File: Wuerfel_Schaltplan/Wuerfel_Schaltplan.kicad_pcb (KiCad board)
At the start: 2 copper layers, 21 parts, among them SW1 SW_Push, SW2 SW_Push

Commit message: Finish PCB design
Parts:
- moved D1 68.3 mm to (97.3, 101.5), turned to 0 degrees
- moved D2 61.5 mm to (104.3, 101.5), turned to 0 degrees
- moved R1 58.2 mm to (118.8, 114.0), turned to 0 degrees
- moved D3 57.7 mm to (111.3, 101.5), turned to 0 degrees
- moved R2 51.3 mm to (118.8, 108.0), turned to 0 degrees
- moved D4 48.2 mm to (104.3, 92.0), turned to 0 degrees
- moved R3 44.0 mm to (118.8, 101.5), turned to 0 degrees
- moved D5 38.6 mm to (111.3, 82.5), turned to 0 degrees
- moved D6 38.3 mm to (104.3, 82.5), turned to 0 degrees
- moved D7 38.0 mm to (97.3, 82.5), turned to 0 degrees
- moved R4 33.9 mm to (118.8, 92.0), turned to 0 degrees
- moved R10 24.4 mm to (212.9, 92.5), turned to 0 degrees
- moved R5 24.0 mm to (118.8, 82.5), turned to 0 degrees
- moved R11 23.7 mm to (200.2, 92.5), turned to 0 degrees
- moved R9 19.6 mm to (222.3, 84.5), turned to 180 degrees
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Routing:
- net Net-(D1-K): track 0.00 -> 156.5 mm
- net Net-(A1-A3): track 0.00 -> 103.6 mm
- net Net-(A1-D8): track 0.00 -> 28.7 mm
- net Net-(D7-A): track 0.00 -> 27.8 mm
- net Net-(D1-A): track 0.00 -> 27.6 mm
- net Net-(A1-D7): track 0.00 -> 25.7 mm
- net Net-(A1-D6): track 0.00 -> 21.1 mm
- net Net-(R8-Pad1): track 0.00 -> 20.3 mm
- net Net-(R10-Pad1): track 0.00 -> 20.3 mm
- net Net-(A1-D5): track 0.00 -> 18.8 mm
- net Net-(D6-A): track 0.00 -> 18.1 mm
- net Net-(D2-A): track 0.00 -> 18.1 mm
- net Net-(A1-D2): track 0.00 -> 15.6 mm
- net Net-(A1-D3): track 0.00 -> 14.2 mm
- net Net-(A1-D4): track 0.00 -> 13.4 mm
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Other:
- board outline added: 146 x 75.5 mm

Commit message: Finish schematic and pcb
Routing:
- net Net-(D1-K): track 156.5 -> 148.8 mm
- net Net-(A1-A3): track 103.6 -> 96.3 mm

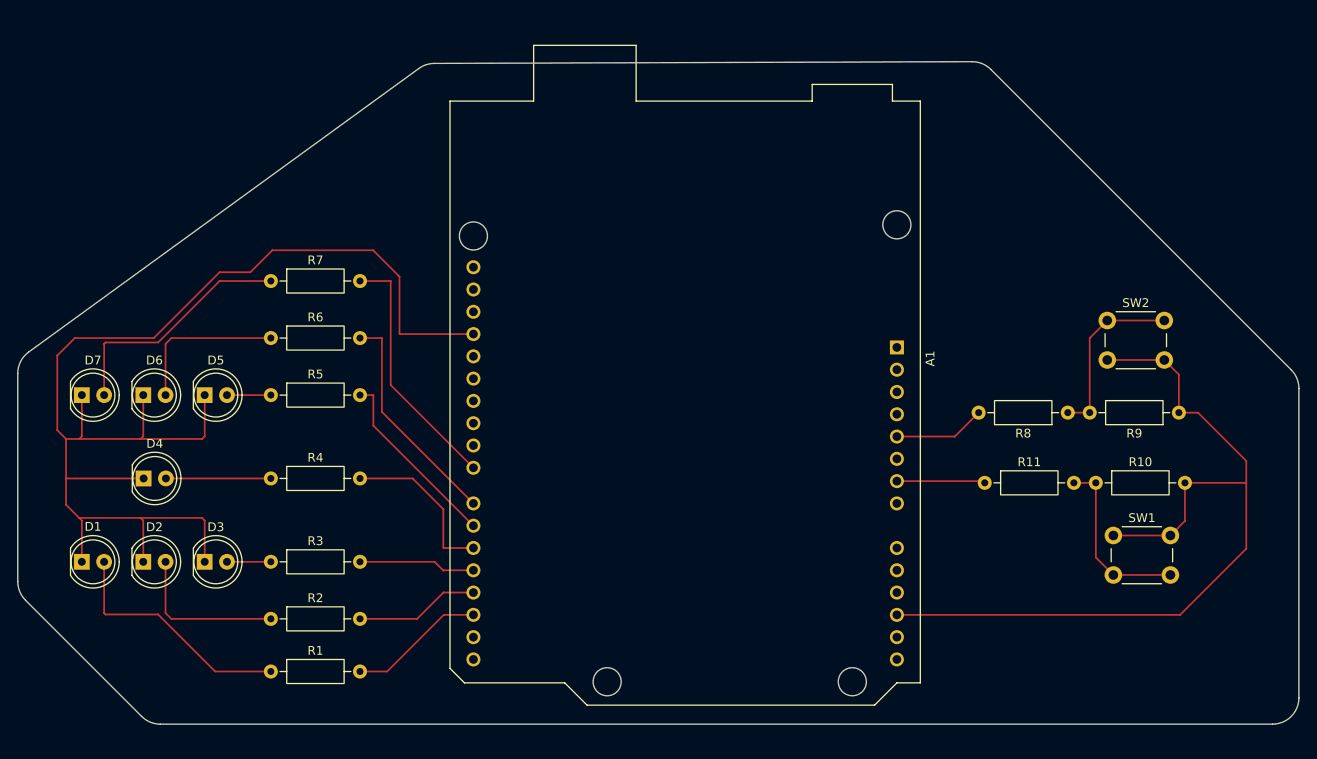
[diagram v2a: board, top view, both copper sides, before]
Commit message: Fix: Cut Edges
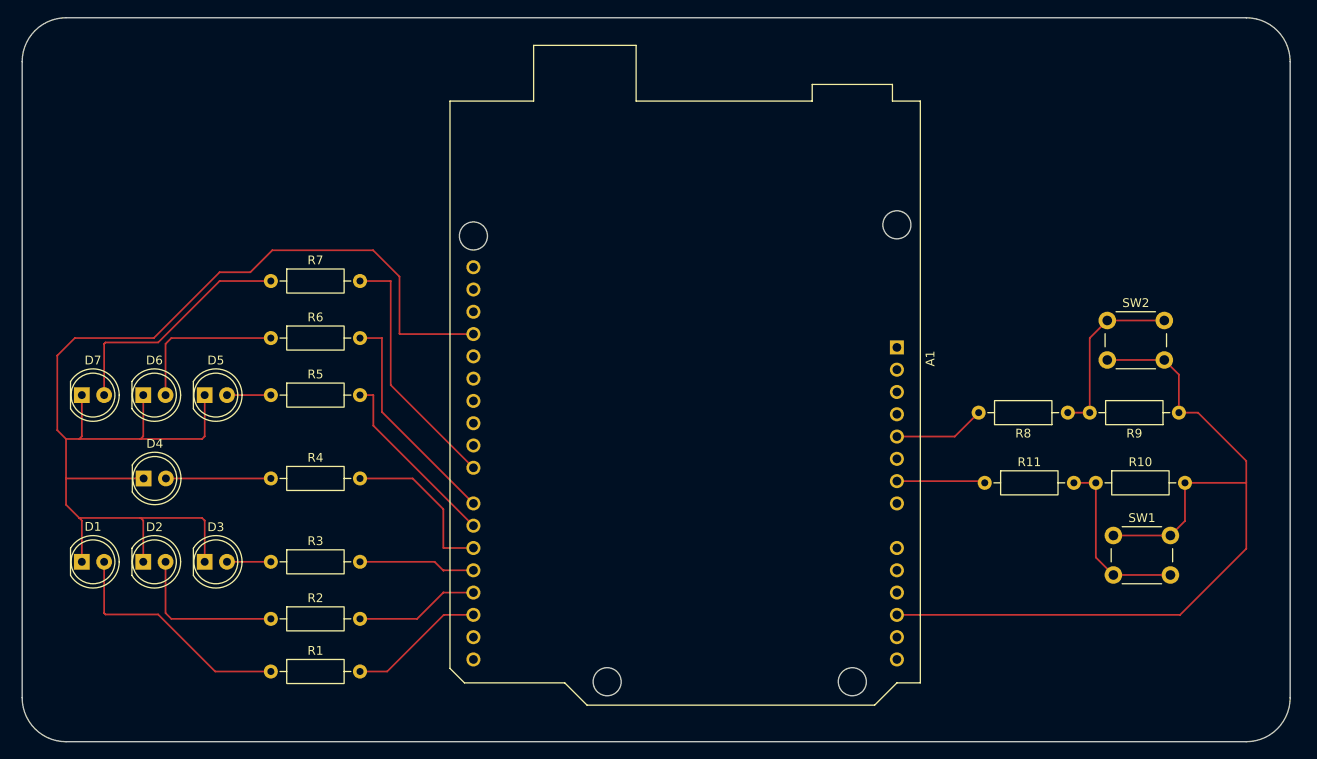
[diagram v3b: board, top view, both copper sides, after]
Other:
- board size 146 x 75.5 mm -> 144.5 x 82.5 mm
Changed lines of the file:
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@@
 	)
 	(gr_arc
-		(start 89.998449 80.028435)
-		(mid 90.325259 78.666523)
-		(end 91.234761 77.601439)
+		(start 90.5 44.5)
+		(mid 91.964466 40.964466)
+		(end 95.5 39.5)
 		(stroke
 			(width 0.05)
@@
 	)
 	(gr_line
-		(start 89.999921 103.757468)
-		(end 89.998449 80.028435)
+		(start 90.5 117)
+		(end 90.5 44.5)
+		(stroke
+			(width 0.05)
+			(type default)
+		)
+		(layer "Edge.Cuts")
+	)
+	(gr_line
+		(start 95.5 39.5)
+		(end 230 39.5)
 		(stroke
 			(width 0.05)
@@
 	)
 	(gr_arc
-		(start 90.8786 105.878602)
-		(mid 90.228319 104.905418)
-		(end 89.999921 103.757468)
+		(start 95.5 122)
+		(mid 91.964466 120.535534)
+		(end 90.5 117)
+		(stroke
+			(width 0.05)
+			(type default)
+		)
+		(layer "Edge.Cuts")
+	)
+	(gr_arc
+		(start 230 39.5)
+		(mid 233.535534 40.964466)
+		(end 235 44.5)
 		(stroke
 			(width 0.05)
@@
 	)
 	(gr_line
-		(start 91.234761 77.601439)
-		(end 135.715622 45.274895)
+		(start 230 122)
+		(end 95.5 122)
 		(stroke
 			(width 0.05)
@@
 	)
 	(gr_line
-		(start 104.121318 119.12132)
-		(end 90.8786 105.878602)
+		(start 235 44.5)
+		(end 235 117)
 		(stroke
 			(width 0.05)
@@
 	)
 	(gr_arc
-		(start 106.242639 120)
-		(mid 105.09458 119.771652)
-		(end 104.121318 119.12132)
+		(start 235 117)
+		(mid 233.535534 120.535534)
+		(end 230 122)
 		(stroke
 			(width 0.05)
-			(type default)
-		)
-		(layer "Edge.Cuts")
-	)
-	(gr_arc
-		(start 135.715622 45.274895)
-		(mid 136.547463 44.850101)
-		(end 137.469632 44.70172)
-		(stroke
-			(width 0.05)
-			(type default)
-		)
-		(layer "Edge.Cuts")
-	)
-	(gr_line
-		(start 137.469632 44.70172)
-		(end 198.751691 44.504027)
-		(stroke
-			(width 0.05)
-			(type default)
-		)
-		(layer "Edge.Cuts")
-	)
-	(gr_arc
-		(start 198.751691 44.504027)
-		(mid 199.904953 44.730516)
-		(end 200.882689 45.382691)
-		(stroke
-			(width 0.05)
-			(type default)
-		)
-		(layer "Edge.Cuts")
-	)
-	(gr_line
-		(start 200.882689 45.382691)
-		(end 235.121319 79.621321)
-		(stroke
-			(width 0.05)
-			(type default)
-		)
-		(layer "Edge.Cuts")
-	)
-	(gr_line
-		(start 232.999998 120)
-		(end 106.242639 120)
-		(stroke
-			(width 0.05)
-			(type default)
-		)
-		(layer "Edge.Cuts")
-	)
-	(gr_arc
-		(start 235.121319 79.621321)
-		(mid 235.771624 80.594593)
-		(end 235.999998 81.742641)
-		(stroke
-			(width 0.05)
-			(type default)
-		)
-		(layer "Edge.Cuts")
-	)
-	(gr_line
-		(start 235.999998 81.742641)
-		(end 235.999998 117)
-		(stroke
-			(width 0.05)
-			(type default)
-		)
-		(layer "Edge.Cuts")
-	)
-	(gr_arc
-		(start 235.999998 117)
-		(mid 235.121318 119.12132)
-		(end 232.999998 120)
-		(stroke
-			(width 0.05)

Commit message: Fix: Change Resitorvalues
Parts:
- R1, R2, R3, R4, R5, R6, R7: value 220 -> 330
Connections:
- net Net-(D1-K) renamed GND
